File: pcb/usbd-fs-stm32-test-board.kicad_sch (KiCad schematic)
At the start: 28 parts, among them J1 USB_B_Mini, J2 USB_B_Mini, U1 USBLC6-2SC6, U2 USBLC6-2SC6

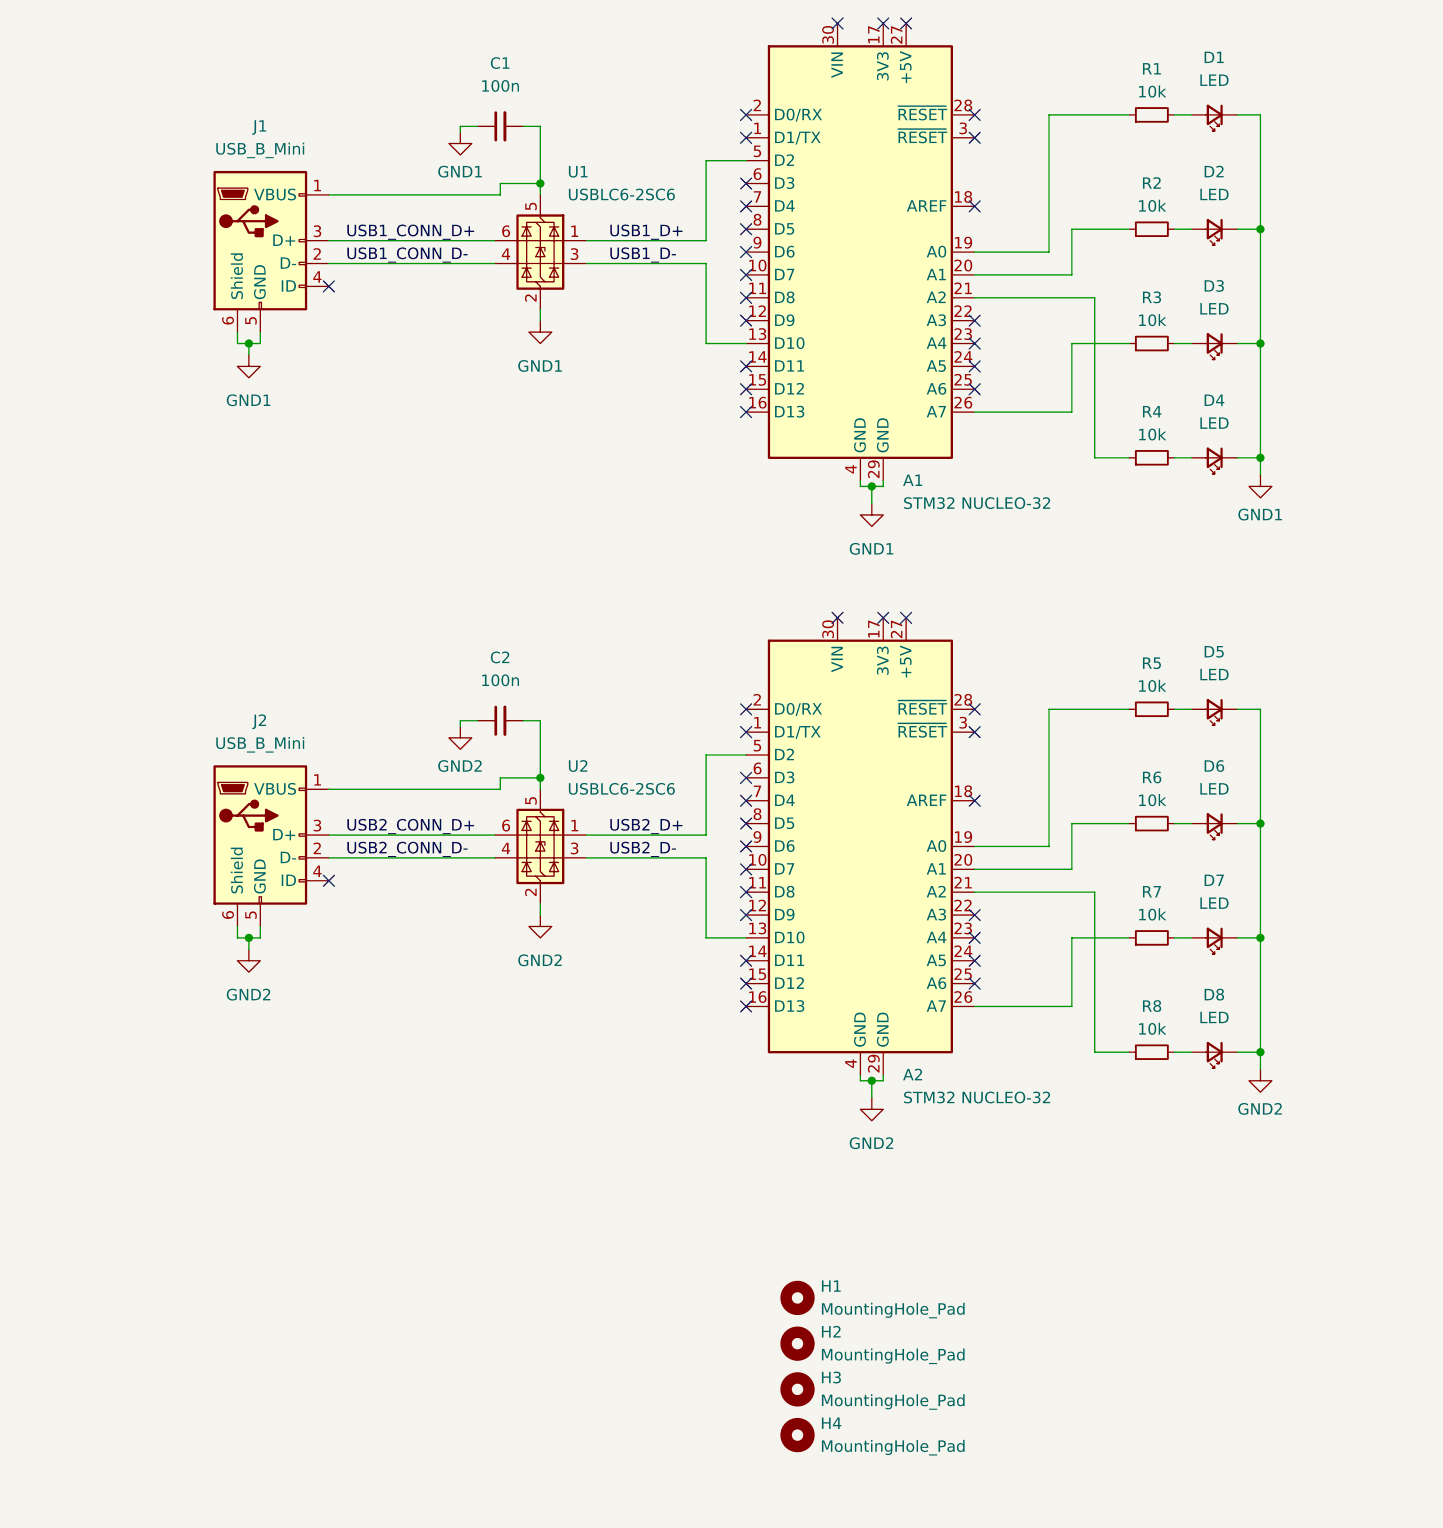
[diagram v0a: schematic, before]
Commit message: pcb: revision 20241120: fixed conflict of LED pins with VCP pins
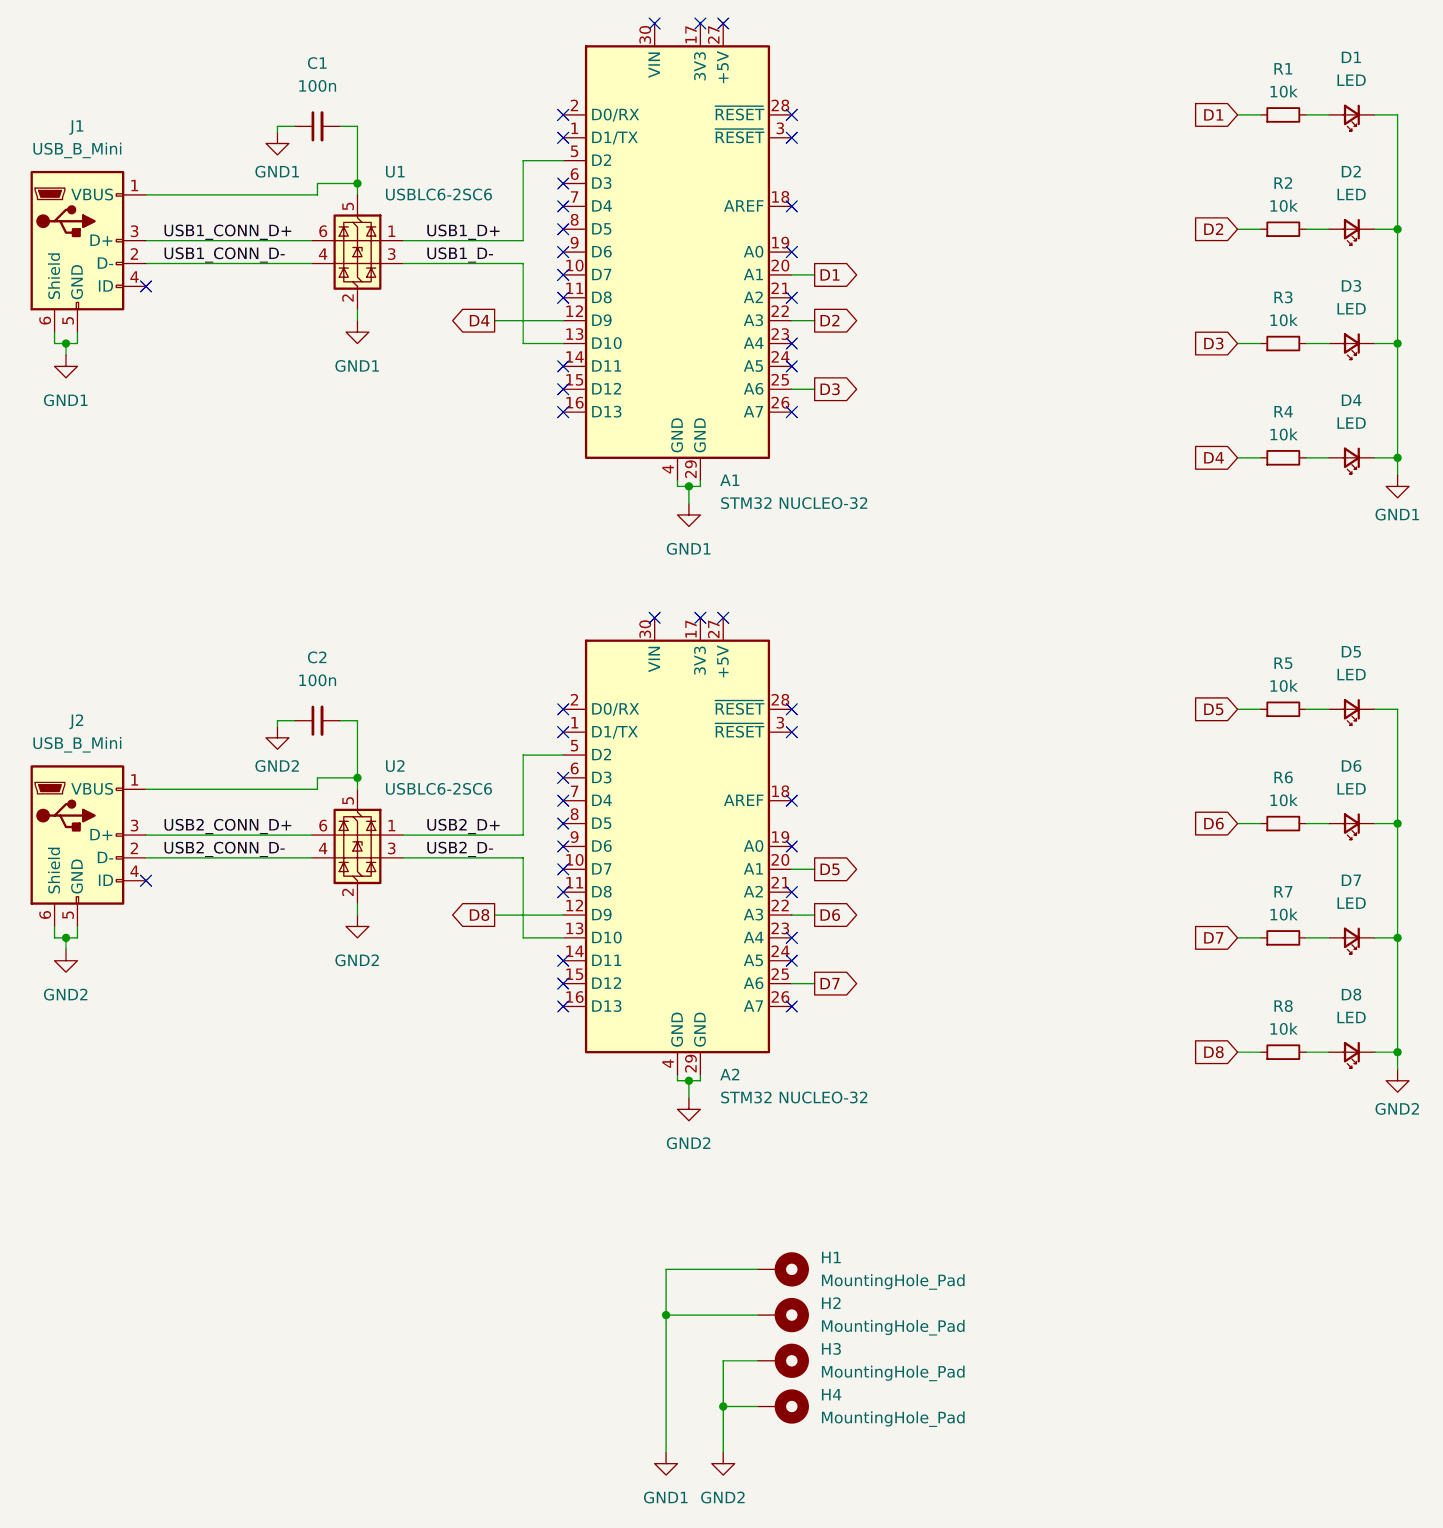
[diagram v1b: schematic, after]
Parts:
- H1, H2, H3, H4: footprint MountingHole:MountingHole_2.2mm_M2 -> MountingHole:MountingHole_2.2mm_M2_Pad_Via; symbol Mechanical:MountingHole -> Mechanical:MountingHole_Pad
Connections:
- net GND1: now also H1.1, H2.1
- net GND2: now also H3.1, H4.1
- net D5: now reaches A2.20 (A1)
- net D5: now also R5.1; no longer R6.1
- net at A2.26 (A7): no longer R7.1
- net at A1.19 (A0): no longer R1.1
- net D8: now reaches A2.12 (D9)
- net D8: now also R8.1
- net at A2.19 (A0): no longer R5.1
- net at A2.21 (A2): no longer R8.1
- net D6: now reaches A2.22 (A3)
- net D6: now also R6.1
- net D7: now reaches A2.25 (A6)
- net D7: now also R7.1
- net D4: now reaches A1.12 (D9)
- net D4: now also R4.1
- net D1: now reaches A1.20 (A1)
- net D1: now also R1.1; no longer R2.1
- net at A1.21 (A2): no longer R4.1
- net D2: now reaches A1.22 (A3)
- net D2: now also R2.1
- net D3: now reaches A1.25 (A6)
- net D3: now also R3.1
- net at A1.26 (A7): no longer R3.1
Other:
- moved on the sheet: A1, A2, C1, C2, D1, D2, D3, D4, D5, D6, D7, D8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
